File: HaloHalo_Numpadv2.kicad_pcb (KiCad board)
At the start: 2 copper layers, 120.5 x 105.4 mm, 99 parts, among them J1 Conn_01x12_Female, J2 Conn_01x12_Female, J3 Conn_01x04_Female, SW1 SW_SPST, SW10 SW_SPST, SW11 SW_SPST, SW12 SW_SPST, SW13 SW_SPST, SW14 SW_SPST, SW15 SW_SPST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

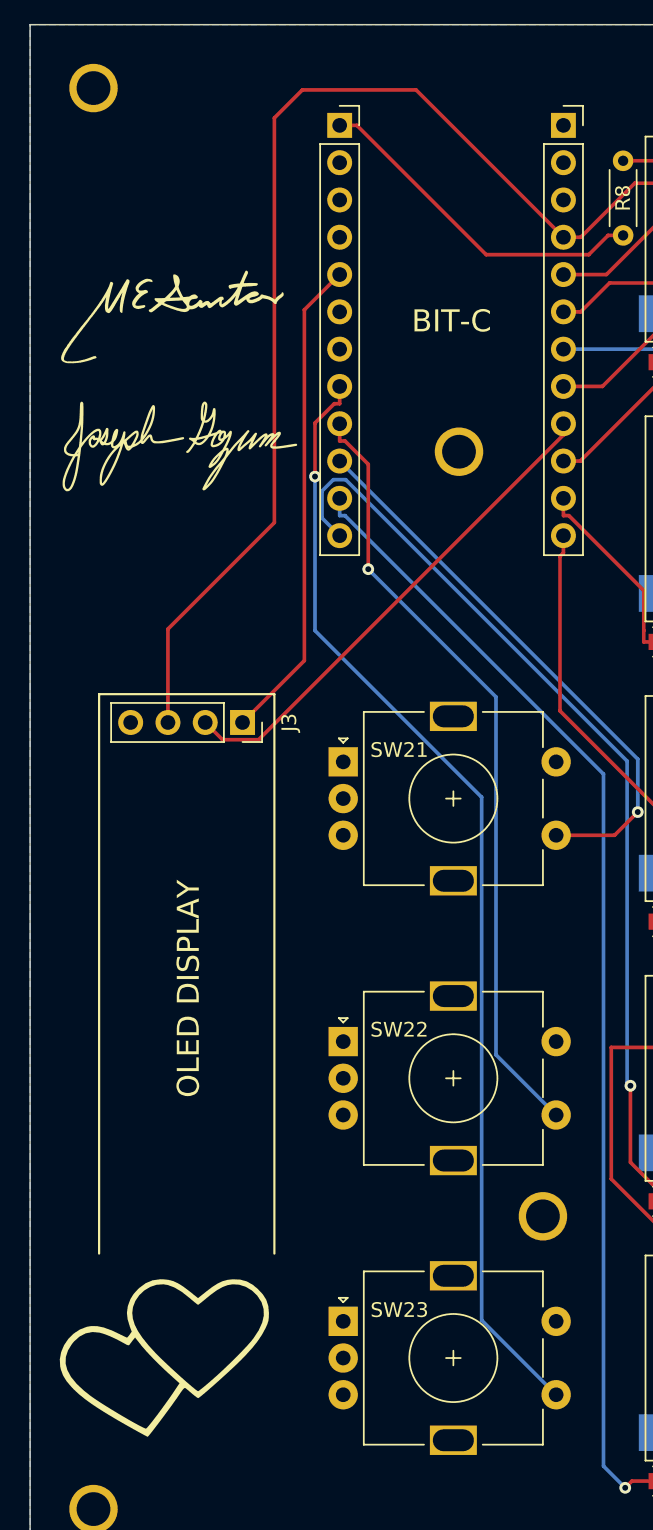
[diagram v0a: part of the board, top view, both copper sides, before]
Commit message: Moved position of display headers in PCB. Started tracking gerbers.zip
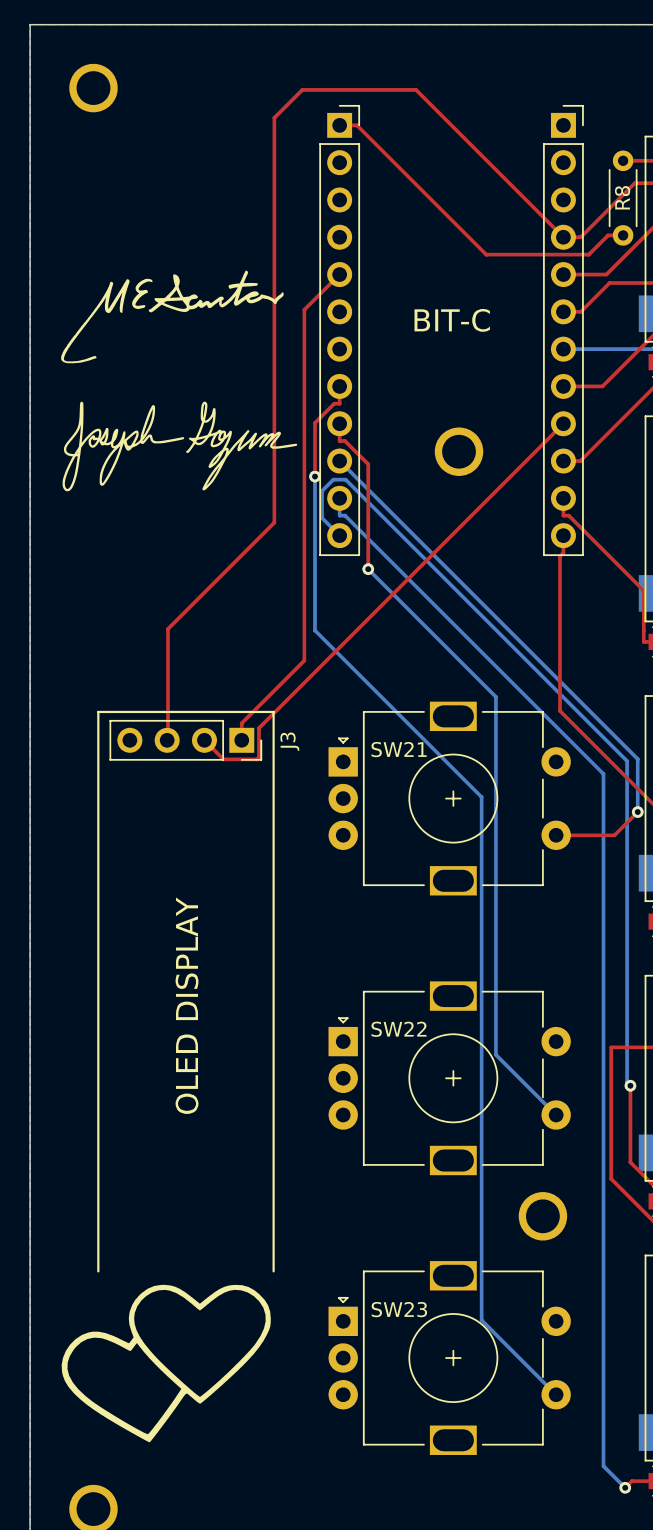
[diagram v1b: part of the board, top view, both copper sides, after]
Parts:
- moved J3 1.21 mm to (88.6, 93.9)
- moved Hearts 0.40 mm to (83.4, 136.2)
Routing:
- net SCL: track 34.2 -> 35.6 mm
- net VCC: track 643.3 -> 644.5 mm
- net SDA: track 33.2 -> 34.5 mm
